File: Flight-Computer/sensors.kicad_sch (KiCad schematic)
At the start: 44 parts, among them P4 440054-3, P5 440054-3, P6 440054-3, P7 440054-3, Q1 QS5U17TR, Q2 QS5U17TR, Q3 QS5U17TR, Q4 QS5U17TR, U12 BMM350, U13 S-85S1AB33-I6T1U, U3 BMI323, U4 MAX-8C-0-10, U5 BMP390

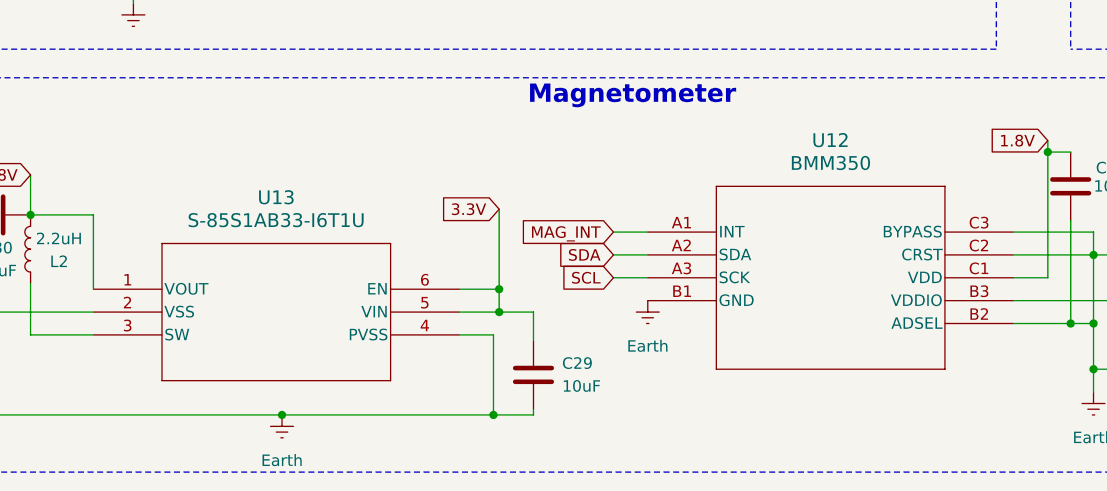
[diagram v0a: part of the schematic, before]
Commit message: New Flash/4x UART
Added Microchip Technologies Flash and 3 more UART peripheral connectors
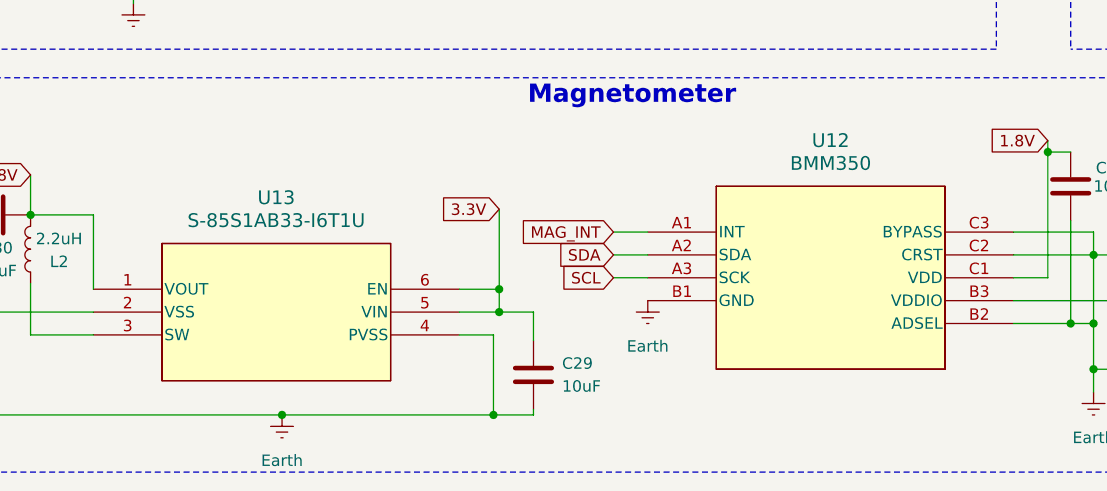
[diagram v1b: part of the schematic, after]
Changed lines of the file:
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@@
 	(label "GPS"
 		(at 27.94 121.285 0)
-		(fields_autoplaced yes)
 		(effects
 			(font
@@
 	(label "3V_BAK"
 		(at 117.475 100.965 0)
-		(fields_autoplaced yes)
 		(effects
 			(font

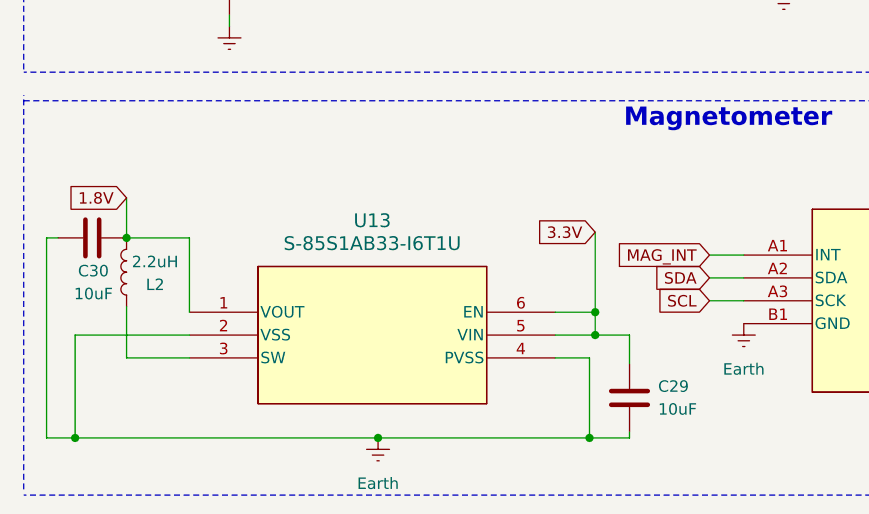
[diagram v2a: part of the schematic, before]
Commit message: LDO update
Changed buck 1.8V converter to LDO
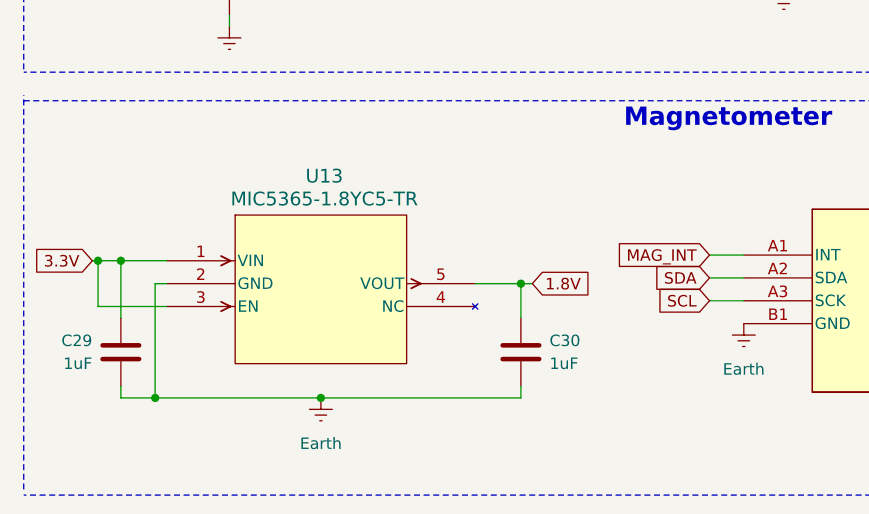
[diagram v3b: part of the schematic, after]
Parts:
- removed L2: 2.2uH, Inductor_SMD:L_0201_0603Metric, symbol Device:L
- removed U13: S-85S1AB33-I6T1U, S85S1A:SNT-6A-A-PKG_PG006-A-P-SD-2.1_ABL, symbol S85S1:S-85S1AB33-I6T1U
- added U13: MIC5365-1.8YC5-TR, MIC5365:SC-70_C5_MCH-L, symbol MIC5365_1_8YC5_TR:MIC5365-1.8YC5-TR
- C29, C30: value 10uF -> 1uF; footprint Capacitor_SMD:C_0201_0603Metric -> Capacitor_SMD:C_0402_1005Metric
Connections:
- net 1.8V: now also C30.1, U13.5 (VOUT); no longer C30.2
- net 3.3V: now also U13.1 (VIN), U13.3 (EN)
- net Earth: now also C30.2, U13.2 (GND); no longer C30.1
